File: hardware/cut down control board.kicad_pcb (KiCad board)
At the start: 2 copper layers, 152.4 x 63.7 mm, 52 parts, among them J1 CUTTER, J10 SAT(10 picoblade), J11 VGPS SELECT, J12 Analog In, J13 EXT BATT, J14 D8 I/O, J2 MOTOR, J3 ISP, J5 SAT(PIN HDR), J6 GPS(PIN HDR)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

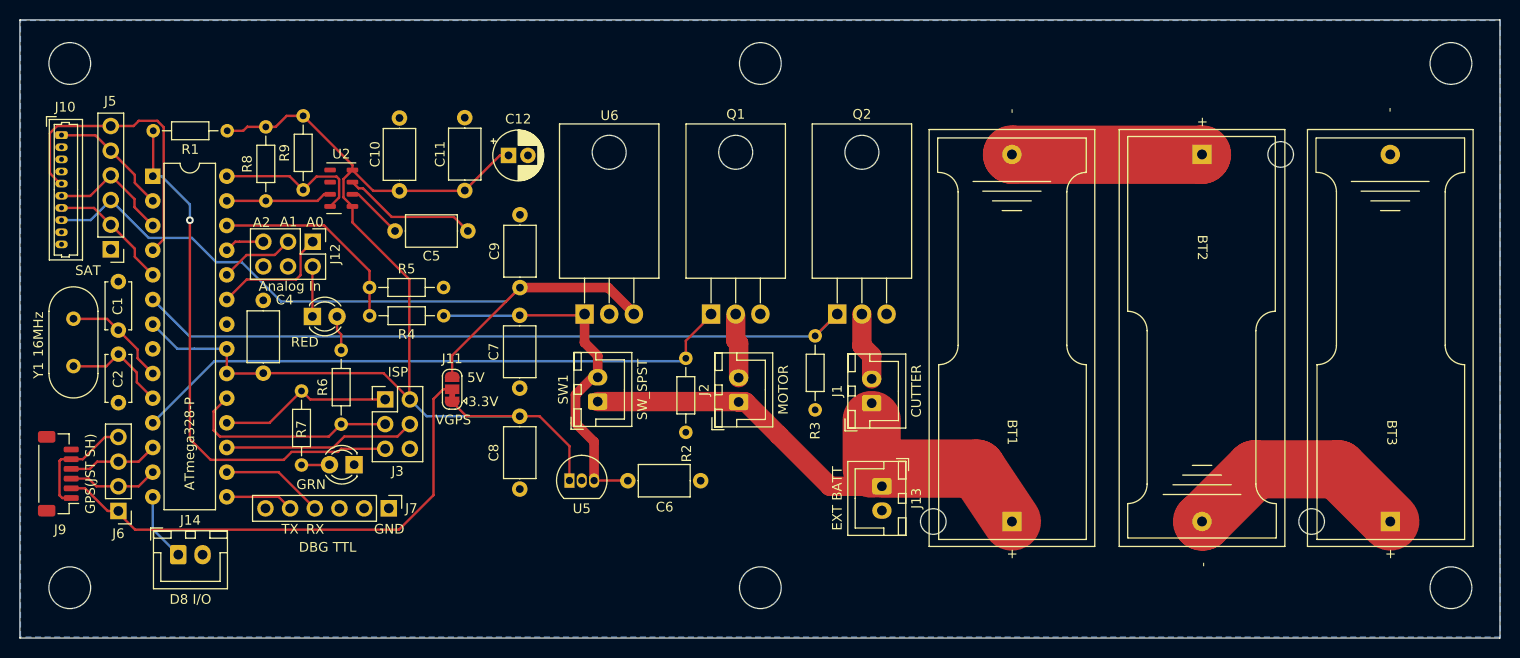
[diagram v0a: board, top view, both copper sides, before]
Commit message: reversed picoblade connector for rockblock 9603
cable pin 1 to pin 10, pin 2 to 9, etc (premade cables are reversed)
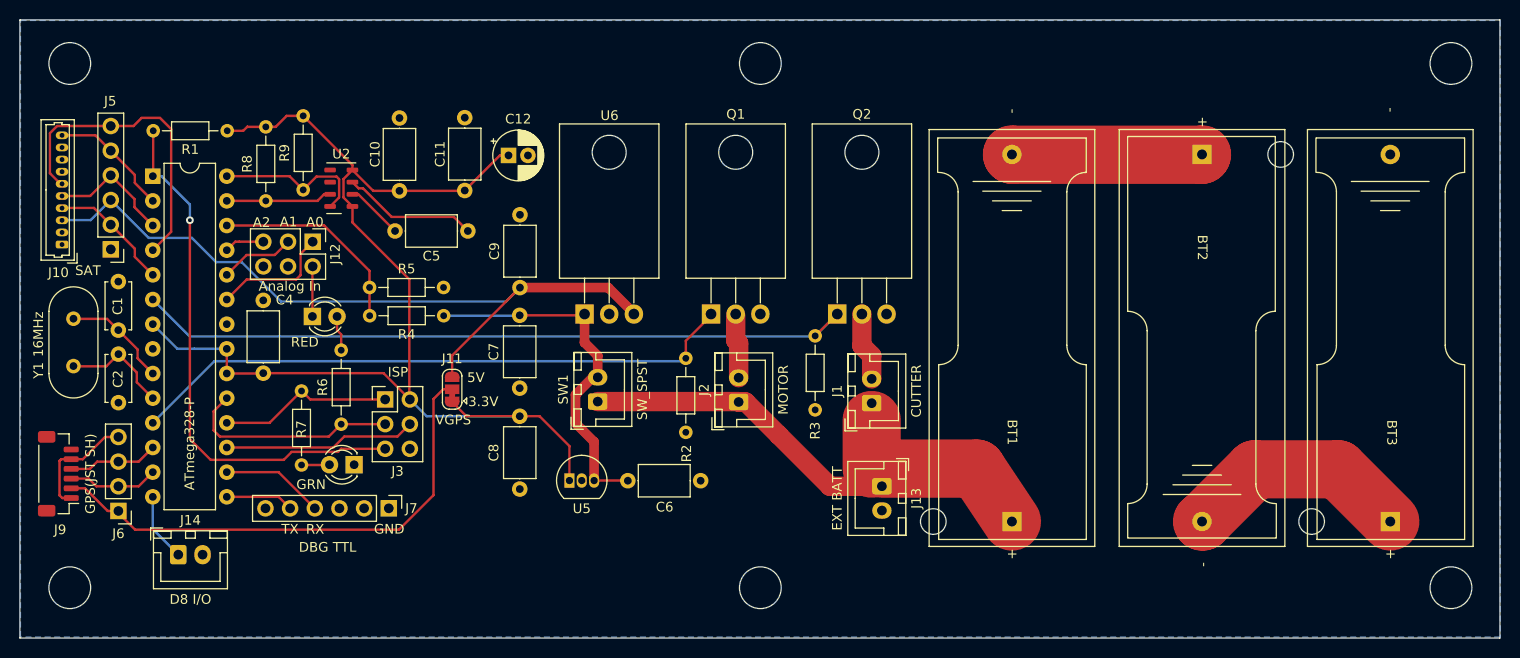
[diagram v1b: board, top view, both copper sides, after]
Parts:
- R6, R7: value 330 -> 130
- moved J10 11.3 mm to (79.9, 90.9), turned to 90 degrees
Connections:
- J10 pad 1: /RX_SAT -> GND
- J10 pad 10: GND -> /RX_SAT
- J10 pad 2: /CTS -> /Li_Ion
- J10 pad 3: /RTS -> +5V
- J10 pad 4: /NetAv -> /SLEEP
- J10 pad 5: /RING -> /TX_SAT
- J10 pad 6: /TX_SAT -> /RING
- J10 pad 7: /SLEEP -> /NetAv
- J10 pad 8: +5V -> /RTS
- J10 pad 9: /Li_Ion -> /CTS
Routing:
- net /RING: track 31.4 -> 32.6 mm

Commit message: remove rockblock sleep from schematic and pcb
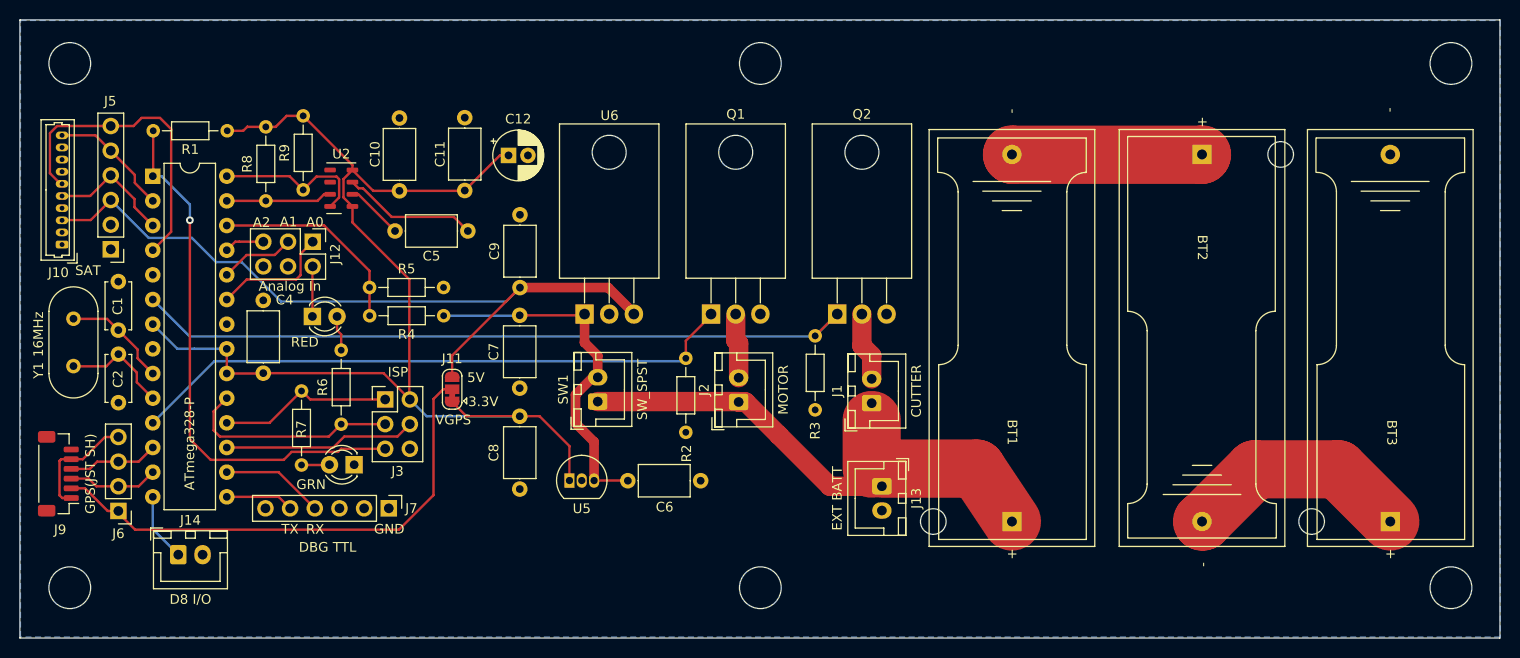
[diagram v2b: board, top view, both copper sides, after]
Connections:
- J10 pad 4: /SLEEP -> unconnected-(J10-Pad4)
- J5 pad 2: /SLEEP -> unconnected-(J5-Pad2)
- U1 pad 5: /SLEEP -> unconnected-(U1-Pad5)
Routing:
- net /SLEEP: track 12.7 -> 0.00 mm
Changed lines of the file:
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@@
   (net 28 "Net-(J2-Pad2)")
   (net 29 "Net-(J1-Pad2)")
-  (net 30 "/SLEEP")
+  (net 30 "unconnected-(J5-Pad2)")
   (net 31 "/1PPS")
   (net 32 "+5V")
@@
   (net 45 "/A1")
   (net 46 "/A2")
+  (net 47 "unconnected-(J10-Pad4)")
+  (net 48 "unconnected-(U1-Pad5)")
   (footprint "Resistor_THT:R_Axial_DIN0204_L3.6mm_D1.6mm_P7.62mm_Horizontal" (layer "F.Cu")
     (at 157.48 100.33 -90)
@@
     (fp_line (start -1.846921 -7.544934) (end -1.846921 7.655066) (layer "F.SilkS") (width 0.12))
     (fp_arc (start 35.953079 -7.544934) (mid 35.367285 -6.130727) (end 33.953079 -5.544934) (layer "F.SilkS") (width 0.12))
-    (fp_arc (start 18.153079 -5.544934) (mid 16.738882 -6.130738) (end 16.153079 -7.544934) (layer "F.SilkS") (width 0.12))
-    (fp_arc (start 33.953079 5.655066) (mid 35.367318 6.240843) (end 35.953079 7.655066) (layer "F.SilkS") (width 0.12))
+    (fp_arc (start 18.153079 -5.544934) (mid 16.738885 -6.130739) (end 16.153079 -7.544934) (layer "F.SilkS") (width 0.12))
+    (fp_arc (start 33.953079 5.655066) (mid 35.367283 6.240849) (end 35.953079 7.655066) (layer "F.SilkS") (width 0.12))
     (fp_arc (start 16.153079 7.655066) (mid 16.738852 6.24084) (end 18.153079 5.655066) (layer "F.SilkS") (width 0.12))
     (fp_line (start 40.5 8.65) (end -2.696921 8.65) (layer "F.CrtYd") (width 0.05))
@@
       (net 32 "+5V") (pinfunction "Pin_3") (pintype "passive"))
     (pad "4" thru_hole oval (at 3.75 0 90) (size 0.8 1.3) (drill 0.5) (layers *.Cu *.Mask)
-      (net 30 "/SLEEP") (pinfunction "Pin_4") (pintype "passive"))
+      (net 47 "unconnected-(J10-Pad4)") (pinfunction "Pin_4") (pintype "passive"))
     (pad "5" thru_hole oval (at 5 0 90) (size 0.8 1.3) (drill 0.5) (layers *.Cu *.Mask)
       (net 7 "/TX_SAT") (pinfunction "Pin_5") (pintype "passive"))
@@
     (fp_line (start 35.953079 -7.65) (end 39.5 -7.65) (layer "F.SilkS") (width 0.12))
     (fp_arc (start 16.153079 7.655066) (mid 16.738852 6.24084) (end 18.153079 5.655066) (layer "F.SilkS") (width 0.12))
-    (fp_arc (start 33.953079 5.655066) (mid 35.367318 6.240843) (end 35.953079 7.655066) (layer "F.SilkS") (width 0.12))
+    (fp_arc (start 33.953079 5.655066) (mid 35.367283 6.240849) (end 35.953079 7.655066) (layer "F.SilkS") (width 0.12))
     (fp_arc (start 35.953079 -7.544934) (mid 35.367285 -6.130727) (end 33.953079 -5.544934) (layer "F.SilkS") (width 0.12))
-    (fp_arc (start 18.153079 -5.544934) (mid 16.738882 -6.130738) (end 16.153079 -7.544934) (layer "F.SilkS") (width 0.12))
+    (fp_arc (start 18.153079 -5.544934) (mid 16.738885 -6.130739) (end 16.153079 -7.544934) (layer "F.SilkS") (width 0.12))
     (fp_line (start -2.696921 -8.65) (end 40.5 -8.65) (layer "F.CrtYd") (width 0.05))
     (fp_line (start 40.5 -8.65) (end 40.5 8.65) (layer "F.CrtYd") (width 0.05))
@@
       (net 4 "GND") (pinfunction "Pin_1") (pintype "passive"))
     (pad "2" thru_hole oval (at 0 2.54 180) (size 1.7 1.7) (drill 1) (layers *.Cu *.Mask)
-      (net 30 "/SLEEP") (pinfunction "Pin_2") (pintype "passive"))
+      (net 30 "unconnected-(J5-Pad2)") (pinfunction "Pin_2") (pintype "passive"))
     (pad "3" thru_hole oval (at 0 5.08 180) (size 1.7 1.7) (drill 1) (layers *.Cu *.Mask)
       (net 32 "+5V") (pinfunction "Pin_3") (pintype "passive"))
@@
       (net 8 "/RING") (pinfunction "PD2") (pintype "bidirectional"))
     (pad "5" thru_hole oval (at 0 10.16) (size 1.6 1.6) (drill 0.8) (layers *.Cu *.Mask)
-      (net 30 "/SLEEP") (pinfunction "PD3") (pintype "bidirectional"))
+      (net 48 "unconnected-(U1-Pad5)") (pinfunction "PD3") (pintype "bidirectional+no_connect"))
     (pad "6" thru_hole oval (at 0 12.7) (size 1.6 1.6) (drill 0.8) (layers *.Cu *.Mask)
       (net 9 "/CUTTER") (pinfunction "PD4") (pintype "bidirectional"))
@@
     (fp_line (start -1.846921 7.655066) (end 16.153079 7.655066) (layer "F.SilkS") (width 0.12))
     (fp_arc (start 35.953079 -7.544934) (mid 35.367285 -6.130727) (end 33.953079 -5.544934) (layer "F.SilkS") (width 0.12))
-    (fp_arc (start 33.953079 5.655066) (mid 35.367318 6.240843) (end 35.953079 7.655066) (layer "F.SilkS") (width 0.12))
+    (fp_arc (start 33.953079 5.655066) (mid 35.367283 6.240849) (end 35.953079 7.655066) (layer "F.SilkS") (width 0.12))
     (fp_arc (start 16.153079 7.655066) (mid 16.738852 6.24084) (end 18.153079 5.655066) (layer "F.SilkS") (width 0.12))
-    (fp_arc (start 18.153079 -5.544934) (mid 16.738882 -6.130738) (end 16.153079 -7.544934) (layer "F.SilkS") (width 0.12))
+    (fp_arc (start 18.153079 -5.544934) (mid 16.738885 -6.130739) (end 16.153079 -7.544934) (layer "F.SilkS") (width 0.12))
     (fp_line (start -2.696921 8.65) (end -2.696921 -8.65) (layer "F.CrtYd") (width 0.05))
     (fp_line (start 40.5 -8.65) (end 40.5 8.65) (layer "F.CrtYd") (width 0.05))
@@
   (segment (start 162.293733 101.362462) (end 162.293733 98.084236) (width 2) (layer "F.Cu") (net 29))
   (segment (start 163.30191 104.761022) (end 163.30191 102.370639) (width 2) (layer "F.Cu") (net 29))
-  (segment (start 87.414026 92.194141) (end 89.265786 94.045901) (width 0.25) (layer "F.Cu") (net 30))
-  (segment (start 87.414026 91.354211) (end 87.414026 92.194141) (width 0.25) (layer "F.Cu") (net 30))
-  (segment (start 79.8685 87.153506) (end 83.213321 87.153506) (width 0.25) (layer "F.Cu") (net 30))
-  (segment (start 84.939322 88.879507) (end 87.414026 91.354211) (width 0.25) (layer "F.Cu") (net 30))
-  (segment (start 83.213321 87.153506) (end 84.939322 88.879507) (width 0.25) (layer "F.Cu") (net 30))
+  (segment (start 79.8685 88.403506) (end 82.875323 88.403506) (width 0.25) (layer "F.Cu") (net 32))
   (segment (start 120.095534 102.342389) (end 127.078479 95.359444) (width 0.25) (layer "F.Cu") (net 32))
   (segment (start 136.170113 95.359444) (end 138.80986 97.999191) (width 1) (layer "F.Cu") (net 32))
   (segment (start 127.078479 95.359444) (end 136.170113 95.359444) (width 1) (layer "F.Cu") (net 32))
+  (segment (start 82.875323 88.403506) (end 84.939322 86.339507) (width 0.25) (layer "F.Cu") (net 32))
   (segment (start 120.095534 104.530843) (end 120.095534 102.342389) (width 0.25) (layer "F.Cu") (net 32))
-  (segment (start 79.8685 88.403506) (end 82.875323 88.403506) (width 0.25) (layer "B.Cu") (net 32))
   (segment (start 98.422579 92.737087) (end 102.472618 96.787126) (width 0.25) (layer "B.Cu") (net 32))
   (segment (start 88.842422 90.242607) (end 93.299792 90.242607) (width 0.25) (layer "B.Cu") (net 32))
-  (segment (start 82.875323 88.403506) (end 84.939322 86.339507) (width 0.25) (layer "B.Cu") (net 32))
   (segment (start 102.472618 96.787126) (end 125.650797 96.787126) (width 0.25) (layer "B.Cu") (net 32))
   (segment (start 84.939322 86.339507) (end 88.842422 90.242607) (width 0.25) (layer "B.Cu") (net 32))
